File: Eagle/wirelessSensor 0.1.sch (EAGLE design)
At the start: 22 parts, among them U1 HDC1080, U2 PIC16F1823-X_SL, X1 22-23-2021

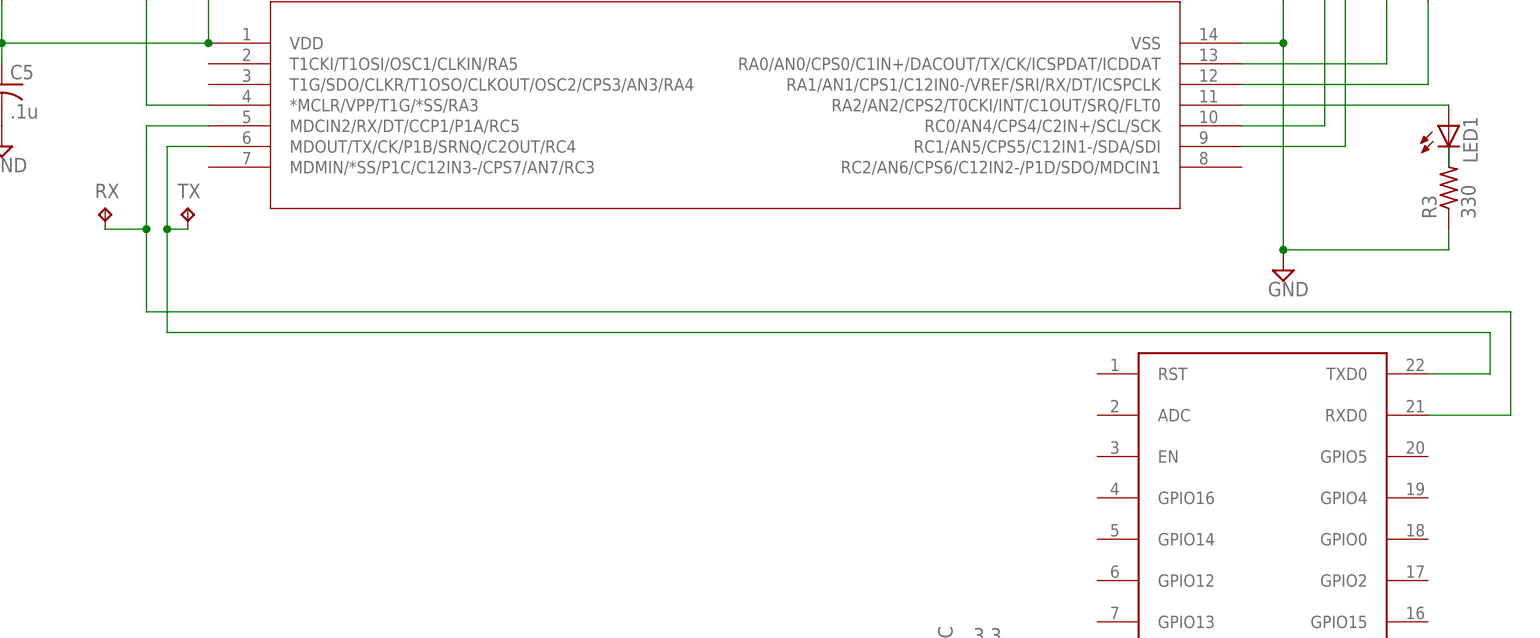
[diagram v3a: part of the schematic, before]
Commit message: Started working on the ESP8266, having some trouble with buffer overrun on the PIC.  Started some board layout
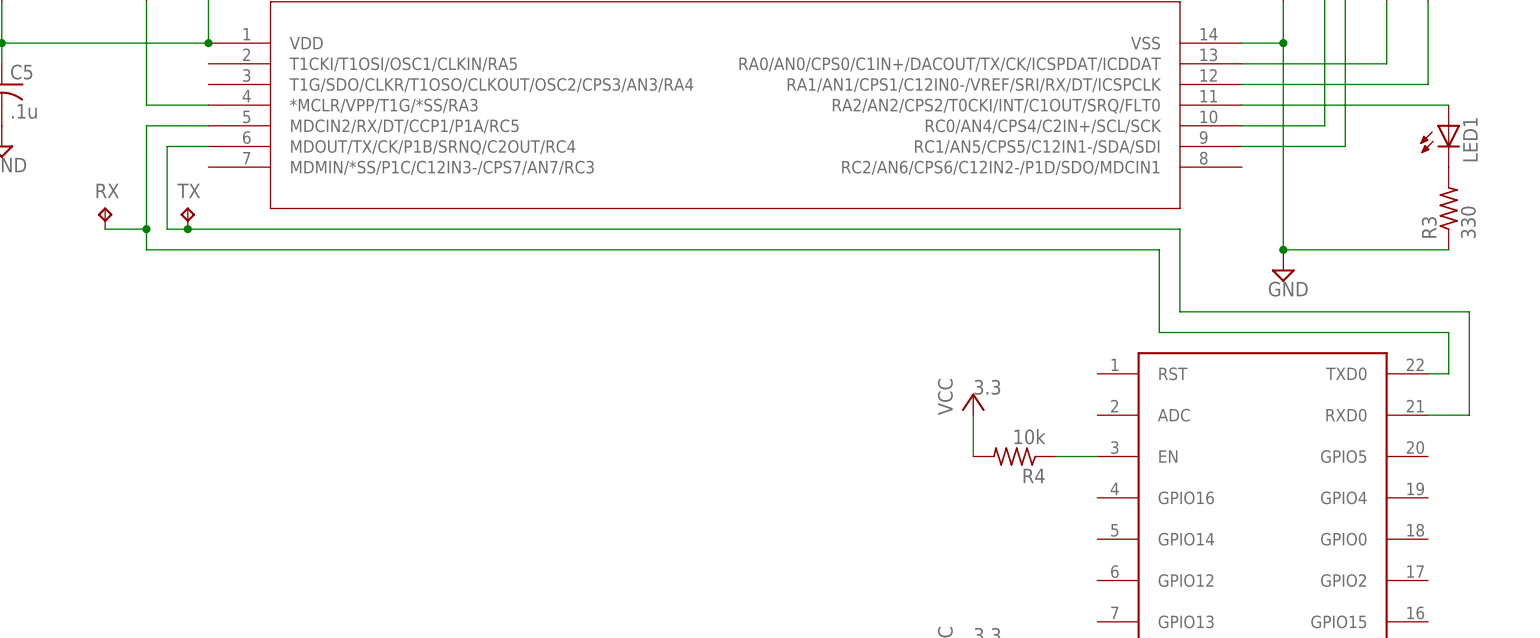
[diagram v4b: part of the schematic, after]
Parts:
- added R4: 10k, rcl:R-US_R0603
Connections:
- new net N$7: R4.1, U$1.EN
- net N$1: now also U$1.TXD0; no longer U$1.RXD0
- net N$8: now also U$1.RXD0; no longer U$1.TXD0
- net VCC: now also R4.2
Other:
- moved on the sheet: R3
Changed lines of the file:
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@@
 <?xml version="1.0" encoding="utf-8"?>
 <!DOCTYPE eagle SYSTEM "eagle.dtd">
-<eagle version="7.7.0">
+<eagle version="7.6.0">
 <drawing>
 <settings>
@@
 </part>
 <part name="SUPPLY5" library="supply2" deviceset="GND" device=""/>
+<part name="R4" library="rcl" deviceset="R-US_" device="R0603" value="10k"/>
+<part name="+3.2" library="supply1" deviceset="VCC" device="">
+<attribute name="VOLTAGE" value="3.3"/>
+</part>
 </parts>
 <sheets>
@@
 <instance part="SUPPLY6" gate="GND" x="-88.9" y="-10.16"/>
 <instance part="LED1" gate="G$1" x="88.9" y="-7.62"/>
-<instance part="R3" gate="G$1" x="88.9" y="-15.24" rot="R90"/>
+<instance part="R3" gate="G$1" x="88.9" y="-17.78" rot="R90"/>
 <instance part="U$1" gate="G$1" x="50.8" y="-88.9"/>
 <instance part="SUPPLY7" gate="GND" x="88.9" y="-78.74"/>
@@
 </instance>
 <instance part="SUPPLY5" gate="GND" x="30.48" y="-91.44"/>
+<instance part="R4" gate="G$1" x="35.56" y="-48.26" rot="R180"/>
+<instance part="+3.2" gate="VCC" x="30.48" y="-40.64">
+<attribute name="VOLTAGE" x="30.48" y="-40.64" size="1.778" layer="96"/>
+</instance>
 </instances>
 <busses>
@@
 <junction x="38.1" y="-73.66"/>
 </segment>
+<segment>
+<pinref part="R4" gate="G$1" pin="2"/>
+<wire x1="30.48" y1="-48.26" x2="30.48" y2="-43.18" width="0.1524" layer="91"/>
+<pinref part="+3.2" gate="VCC" pin="VCC"/>
+</segment>
 </net>
 <net name="GND" class="0">
@@
 <junction x="68.58" y="-22.86"/>
 <pinref part="R3" gate="G$1" pin="1"/>
-<wire x1="88.9" y1="-22.86" x2="88.9" y2="-20.32" width="0.1524" layer="91"/>
 </segment>
 <segment>
@@
 <pinref part="LED1" gate="G$1" pin="C"/>
 <pinref part="R3" gate="G$1" pin="2"/>
-<wire x1="88.9" y1="-10.16" x2="88.9" y2="-12.7" width="0.1524" layer="91"/>
 </segment>
 </net>
 <net name="N$8" class="0">
 <segment>
-<pinref part="U$1" gate="G$1" pin="TXD0"/>
-<wire x1="86.36" y1="-38.1" x2="93.98" y2="-38.1" width="0.1524" layer="91"/>
-<wire x1="93.98" y1="-38.1" x2="93.98" y2="-33.02" width="0.1524" layer="91"/>
-<wire x1="93.98" y1="-33.02" x2="-68.58" y2="-33.02" width="0.1524" layer="91"/>
-<wire x1="-68.58" y1="-33.02" x2="-68.58" y2="-20.32" width="0.1524" layer="91"/>
 <pinref part="U2" gate="A" pin="MDOUT/TX/CK/P1B/SRNQ/C2OUT/RC4"/>
 <wire x1="-68.58" y1="-20.32" x2="-68.58" y2="-10.16" width="0.1524" layer="91"/>
@@
 <pinref part="TX" gate="G$1" pin="TP"/>
 <wire x1="-66.04" y1="-20.32" x2="-68.58" y2="-20.32" width="0.1524" layer="91"/>
-<junction x="-68.58" y="-20.32"/>
+<wire x1="-66.04" y1="-20.32" x2="55.88" y2="-20.32" width="0.1524" layer="91"/>
+<wire x1="55.88" y1="-20.32" x2="55.88" y2="-30.48" width="0.1524" layer="91"/>
+<junction x="-66.04" y="-20.32"/>
+<wire x1="55.88" y1="-30.48" x2="91.44" y2="-30.48" width="0.1524" layer="91"/>
+<wire x1="91.44" y1="-30.48" x2="91.44" y2="-43.18" width="0.1524" layer="91"/>
+<pinref part="U$1" gate="G$1" pin="RXD0"/>
+<wire x1="91.44" y1="-43.18" x2="86.36" y2="-43.18" width="0.1524" layer="91"/>
 </segment>
 </net>
@@
 <wire x1="-71.12" y1="-20.32" x2="-71.12" y2="-7.62" width="0.1524" layer="91"/>
 <wire x1="-71.12" y1="-7.62" x2="-63.5" y2="-7.62" width="0.1524" layer="91"/>
-<wire x1="-71.12" y1="-20.32" x2="-71.12" y2="-30.48" width="0.1524" layer="91"/>
+<wire x1="-71.12" y1="-20.32" x2="-71.12" y2="-22.86" width="0.1524" layer="91"/>
 <junction x="-71.12" y="-20.32"/>
-<wire x1="-71.12" y1="-30.48" x2="96.52" y2="-30.48" width="0.1524" layer="91"/>
-<wire x1="96.52" y1="-30.48" x2="96.52" y2="-43.18" width="0.1524" layer="91"/>
-<pinref part="U$1" gate="G$1" pin="RXD0"/>
-<wire x1="96.52" y1="-43.18" x2="86.36" y2="-43.18" width="0.1524" layer="91"/>
-</segment>
-</net>
+<wire x1="-71.12" y1="-22.86" x2="53.34" y2="-22.86" width="0.1524" layer="91"/>
+<wire x1="53.34" y1="-22.86" x2="53.34" y2="-33.02" width="0.1524" layer="91"/>
+<wire x1="53.34" y1="-33.02" x2="88.9" y2="-33.02" width="0.1524" layer="91"/>
+<wire x1="88.9" y1="-33.02" x2="88.9" y2="-38.1" width="0.1524" layer="91"/>
+<pinref part="U$1" gate="G$1" pin="TXD0"/>
+<wire x1="88.9" y1="-38.1" x2="86.36" y2="-38.1" width="0.1524" layer="91"/>
+</segment>
+</net>
+<net name="N$7" class="0">
+<segment>
+<pinref part="R4" gate="G$1" pin="1"/>
+<pinref part="U$1" gate="G$1" pin="EN"/>
+<wire x1="40.64" y1="-48.26" x2="45.72" y2="-48.26" width="0.1524" layer="91"/>
+</segment>
+</net>

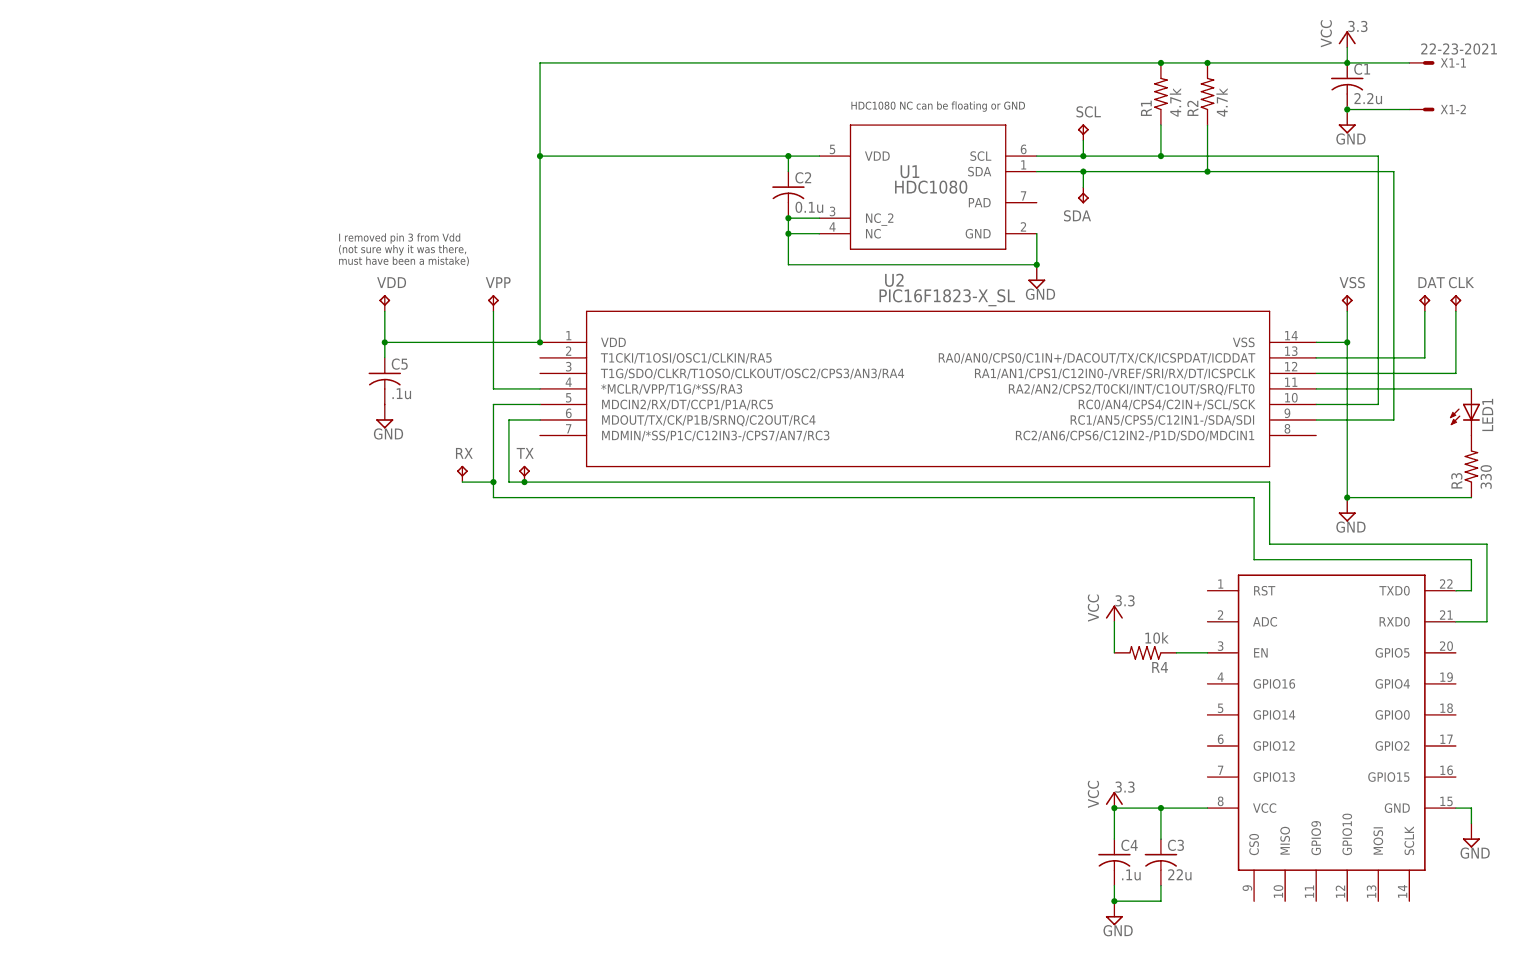
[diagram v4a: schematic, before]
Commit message: Wrapping up the schematic before board order; minor firmware adjustments; added CAM file for Gerber generation
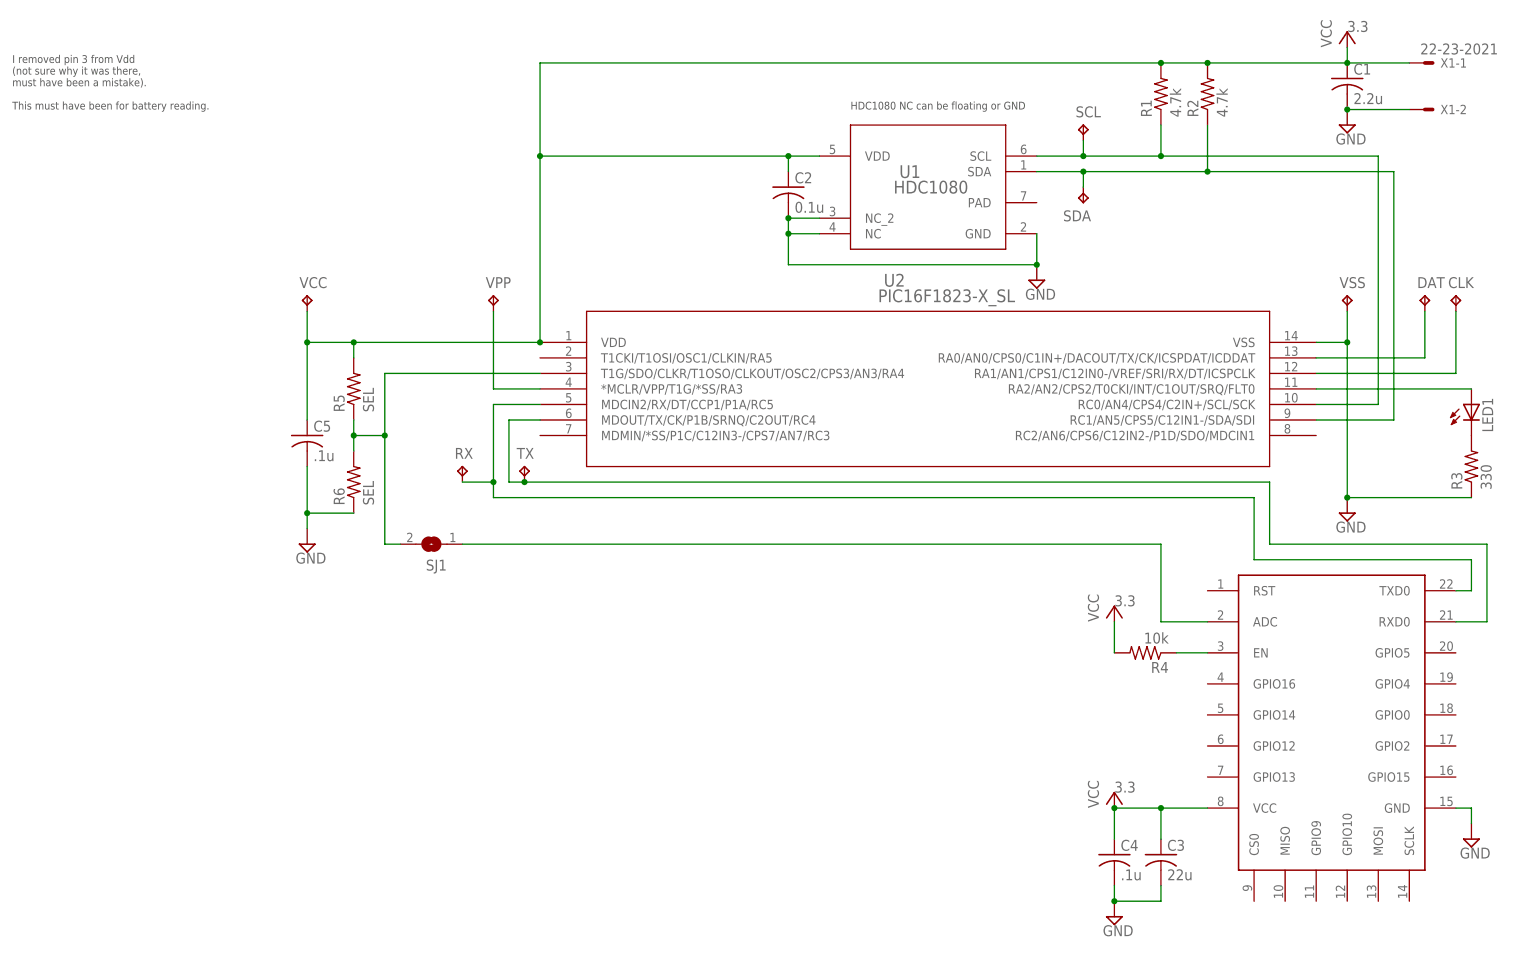
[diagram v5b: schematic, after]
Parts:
- removed VDD: TPB1,27, testpad:TPB1,27
- added R5, R6: SEL, rcl:R-US_R0603
- added SJ1: (no value), jumper:SJ
- added VCC: TPB1,27, testpad:TPB1,27
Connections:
- new net N$12: SJ1.1, U$1.ADC
- new net N$9: R5.1, R6.2, SJ1.2, U2.T1G/SDO/CLKR/T1OSO/CLKOUT/OSC2/CPS3/AN3/RA4
- net GND: now also R6.1
- net VCC: now also R5.2, VCC.TP; no longer VDD.TP
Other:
- note added: "I removed pin 3 from Vdd (not sure why it was there, must have been a mistake). This must have been for battery reading."
- note removed: "I removed pin 3 from Vdd (not sure why it was there, must have been a mistake)"
- moved on the sheet: C5
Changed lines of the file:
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@@
 <?xml version="1.0" encoding="utf-8"?>
 <!DOCTYPE eagle SYSTEM "eagle.dtd">
-<eagle version="7.6.0">
+<eagle version="7.7.0">
 <drawing>
 <settings>
@@
 <part name="SUPPLY2" library="supply2" deviceset="GND" device=""/>
 <part name="VPP" library="testpad" deviceset="TP" device="B1,27"/>
-<part name="VDD" library="testpad" deviceset="TP" device="B1,27"/>
+<part name="VCC" library="testpad" deviceset="TP" device="B1,27"/>
 <part name="VSS" library="testpad" deviceset="TP" device="B1,27"/>
 <part name="DAT" library="testpad" deviceset="TP" device="B1,27"/>
@@
 <attribute name="VOLTAGE" value="3.3"/>
 </part>
+<part name="R5" library="rcl" deviceset="R-US_" device="R0603" value="SEL"/>
+<part name="R6" library="rcl" deviceset="R-US_" device="R0603" value="SEL"/>
+<part name="SJ1" library="jumper" deviceset="SJ" device=""/>
 </parts>
 <sheets>
 <sheet>
 <plain>
-<text x="-96.52" y="15.24" size="1.27" layer="97">I removed pin 3 from Vdd
+<text x="-149.86" y="40.64" size="1.27" layer="97">I removed pin 3 from Vdd
 (not sure why it was there,
-must have been a mistake)</text>
+must have been a mistake).
+This must have been for battery reading.</text>
 <text x="-12.7" y="40.64" size="1.27" layer="97">HDC1080 NC can be floating or GND</text>
 </plain>
@@
 <instance part="SUPPLY2" gate="GND" x="17.78" y="12.7"/>
 <instance part="VPP" gate="G$1" x="-71.12" y="10.16"/>
-<instance part="VDD" gate="G$1" x="-88.9" y="10.16"/>
+<instance part="VCC" gate="G$1" x="-101.6" y="10.16"/>
 <instance part="VSS" gate="G$1" x="68.58" y="10.16"/>
 <instance part="DAT" gate="G$1" x="81.28" y="10.16"/>
@@
 <instance part="C3" gate="G$1" x="38.1" y="-81.28"/>
 <instance part="C4" gate="G$1" x="30.48" y="-81.28"/>
-<instance part="C5" gate="G$1" x="-88.9" y="-2.54"/>
-<instance part="SUPPLY6" gate="GND" x="-88.9" y="-10.16"/>
+<instance part="C5" gate="G$1" x="-101.6" y="-12.7"/>
+<instance part="SUPPLY6" gate="GND" x="-101.6" y="-30.48"/>
 <instance part="LED1" gate="G$1" x="88.9" y="-7.62"/>
 <instance part="R3" gate="G$1" x="88.9" y="-17.78" rot="R90"/>
@@
 <attribute name="VOLTAGE" x="30.48" y="-40.64" size="1.778" layer="96"/>
 </instance>
+<instance part="R5" gate="G$1" x="-93.98" y="-5.08" rot="R90"/>
+<instance part="R6" gate="G$1" x="-93.98" y="-20.32" rot="R90"/>
+<instance part="SJ1" gate="1" x="-81.28" y="-30.48" rot="R180"/>
 </instances>
 <busses>
@@
 <wire x1="-63.5" y1="33.02" x2="-22.86" y2="33.02" width="0.1524" layer="91"/>
 <wire x1="-22.86" y1="33.02" x2="-17.78" y2="33.02" width="0.1524" layer="91"/>
-<wire x1="-63.5" y1="2.54" x2="-88.9" y2="2.54" width="0.1524" layer="91"/>
+<wire x1="-63.5" y1="2.54" x2="-93.98" y2="2.54" width="0.1524" layer="91"/>
 <junction x="-63.5" y="2.54"/>
-<pinref part="VDD" gate="G$1" pin="TP"/>
-<wire x1="-88.9" y1="2.54" x2="-88.9" y2="7.62" width="0.1524" layer="91"/>
+<pinref part="VCC" gate="G$1" pin="TP"/>
+<wire x1="-93.98" y1="2.54" x2="-101.6" y2="2.54" width="0.1524" layer="91"/>
+<wire x1="-101.6" y1="2.54" x2="-101.6" y2="7.62" width="0.1524" layer="91"/>
 <pinref part="C2" gate="G$1" pin="1"/>
 <wire x1="-22.86" y1="33.02" x2="-22.86" y2="30.48" width="0.1524" layer="91"/>
@@
 <junction x="38.1" y="48.26"/>
 <pinref part="C5" gate="G$1" pin="1"/>
-<wire x1="-88.9" y1="2.54" x2="-88.9" y2="0" width="0.1524" layer="91"/>
-<junction x="-88.9" y="2.54"/>
+<wire x1="-101.6" y1="2.54" x2="-101.6" y2="-10.16" width="0.1524" layer="91"/>
+<junction x="-101.6" y="2.54"/>
+<pinref part="R5" gate="G$1" pin="2"/>
+<wire x1="-93.98" y1="0" x2="-93.98" y2="2.54" width="0.1524" layer="91"/>
+<junction x="-93.98" y="2.54"/>
 </segment>
 <segment>
@@
 <pinref part="C5" gate="G$1" pin="2"/>
 <pinref part="SUPPLY6" gate="GND" pin="GND"/>
+<wire x1="-101.6" y1="-27.94" x2="-101.6" y2="-25.4" width="0.1524" layer="91"/>
+<pinref part="R6" gate="G$1" pin="1"/>
+<wire x1="-101.6" y1="-25.4" x2="-101.6" y2="-17.78" width="0.1524" layer="91"/>
+<wire x1="-101.6" y1="-25.4" x2="-93.98" y2="-25.4" width="0.1524" layer="91"/>
+<junction x="-101.6" y="-25.4"/>
 </segment>
 <segment>
@@
 </segment>
 </net>
+<net name="N$9" class="0">
+<segment>
+<pinref part="R6" gate="G$1" pin="2"/>
+<pinref part="R5" gate="G$1" pin="1"/>
+<wire x1="-93.98" y1="-15.24" x2="-93.98" y2="-12.7" width="0.1524" layer="91"/>
+<wire x1="-93.98" y1="-12.7" x2="-93.98" y2="-10.16" width="0.1524" layer="91"/>
+<wire x1="-93.98" y1="-12.7" x2="-88.9" y2="-12.7" width="0.1524" layer="91"/>
+<junction x="-93.98" y="-12.7"/>
+<wire x1="-88.9" y1="-12.7" x2="-88.9" y2="-2.54" width="0.1524" layer="91"/>
+<pinref part="U2" gate="A" pin="T1G/SDO/CLKR/T1OSO/CLKOUT/OSC2/CPS3/AN3/RA4"/>
+<wire x1="-88.9" y1="-2.54" x2="-63.5" y2="-2.54" width="0.1524" layer="91"/>
+<pinref part="SJ1" gate="1" pin="2"/>
+<wire x1="-88.9" y1="-12.7" x2="-88.9" y2="-30.48" width="0.1524" layer="91"/>
+<wire x1="-88.9" y1="-30.48" x2="-86.36" y2="-30.48" width="0.1524" layer="91"/>
+<junction x="-88.9" y="-12.7"/>
+</segment>
+</net>
+<net name="N$12" class="0">
+<segment>
+<pinref part="SJ1" gate="1" pin="1"/>
+<wire x1="-76.2" y1="-30.48" x2="38.1" y2="-30.48" width="0.1524" layer="91"/>
+<wire x1="38.1" y1="-30.48" x2="38.1" y2="-43.18" width="0.1524" layer="91"/>
+<pinref part="U$1" gate="G$1" pin="ADC"/>
+<wire x1="38.1" y1="-43.18" x2="45.72" y2="-43.18" width="0.1524" layer="91"/>
+</segment>
+</net>
